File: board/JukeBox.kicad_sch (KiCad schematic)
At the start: 38 parts, among them J1 USB_C_Receptacle_USB2.0, SW1 SW_SPST, SW10 SW_SPST, SW11 SW_SPST, SW12 SW_SPST, SW2 SW_SPST, SW3 SW_SPST, SW4 SW_SPST, SW5 SW_SPST, SW6 SW_SPST, SW7 SW_SPST, SW8 SW_SPST, SW9 SW_SPST, U1 ATmega8U2-A, Y1 16MHz

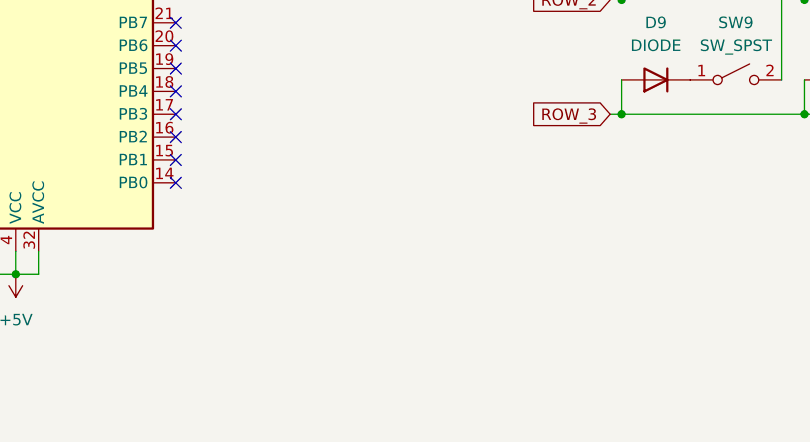
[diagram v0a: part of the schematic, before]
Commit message: update naming, add headers for direct connection
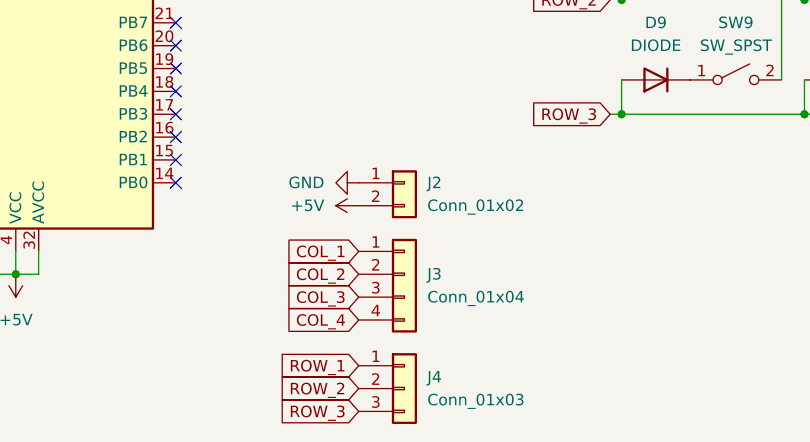
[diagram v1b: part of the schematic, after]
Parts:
- added J2: Conn_01x02, Connector_PinHeader_2.54mm:PinHeader_1x02_P2.54mm_Vertical, symbol Connector_Generic:Conn_01x02
- added J3: Conn_01x04, Connector_PinHeader_2.54mm:PinHeader_1x04_P2.54mm_Vertical, symbol Connector_Generic:Conn_01x04
- added J4: Conn_01x03, Connector_PinHeader_2.54mm:PinHeader_1x03_P2.54mm_Vertical, symbol Connector_Generic:Conn_01x03
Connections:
- net +5V: now also J2.2 (Pin_2)
- net COL_1: now also J3.1 (Pin_1)
- net COL_2: now also J3.2 (Pin_2)
- net COL_3: now also J3.3 (Pin_3)
- net COL_4: now also J3.4 (Pin_4)
- net GND: now also J2.1 (Pin_1)
- net ROW_1: now also J4.1 (Pin_1)
- net ROW_2: now also J4.2 (Pin_2)
- net ROW_3: now also J4.3 (Pin_3)
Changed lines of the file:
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@@
     (effects (font (size 1.27 1.27)) (justify left bottom))
+  )
+  (global_label "COL_4" (shape input) (at 158.75 111.76 180) (fields_autoplaced)
+    (effects (font (size 1.27 1.27)) (justify right))
+    (property "Intersheet References" "${INTERSHEET_REFS}" (id 0) (at 150.5312 111.6806 0)
+      (effects (font (size 1.27 1.27)) (justify right) hide)
+    )
   )
   (global_label "COL_1" (shape input) (at 138.43 53.34 0) (fields_autoplaced)
@@
     )
   )
+  (global_label "ROW_3" (shape input) (at 158.75 121.92 180) (fields_autoplaced)
+    (effects (font (size 1.27 1.27)) (justify right))
+    (property "Intersheet References" "${INTERSHEET_REFS}" (id 0) (at 150.1079 121.8406 0)
+      (effects (font (size 1.27 1.27)) (justify right) hide)
+    )
+  )
   (global_label "COL_2" (shape input) (at 224.79 49.53 180) (fields_autoplaced)
     (effects (font (size 1.27 1.27)) (justify right))
@@
     )
   )
+  (global_label "COL_2" (shape input) (at 158.75 106.68 180) (fields_autoplaced)
+    (effects (font (size 1.27 1.27)) (justify right))
+    (property "Intersheet References" "${INTERSHEET_REFS}" (id 0) (at 150.5312 106.6006 0)
+      (effects (font (size 1.27 1.27)) (justify right) hide)
+    )
+  )
   (global_label "ROW_2" (shape input) (at 186.69 76.2 180) (fields_autoplaced)
     (effects (font (size 1.27 1.27)) (justify right))
     (property "Intersheet References" "${INTERSHEET_REFS}" (id 0) (at 178.0479 76.1206 0)
+      (effects (font (size 1.27 1.27)) (justify right) hide)
+    )
+  )
+  (global_label "COL_1" (shape input) (at 158.75 104.14 180) (fields_autoplaced)
+    (effects (font (size 1.27 1.27)) (justify right))
+    (property "Intersheet References" "${INTERSHEET_REFS}" (id 0) (at 150.5312 104.0606 0)
+      (effects (font (size 1.27 1.27)) (justify right) hide)
+    )
+  )
+  (global_label "ROW_1" (shape input) (at 158.75 116.84 180) (fields_autoplaced)
+    (effects (font (size 1.27 1.27)) (justify right))
+    (property "Intersheet References" "${INTERSHEET_REFS}" (id 0) (at 150.1079 116.7606 0)
+      (effects (font (size 1.27 1.27)) (justify right) hide)
+    )
+  )
+  (global_label "COL_3" (shape input) (at 158.75 109.22 180) (fields_autoplaced)
+    (effects (font (size 1.27 1.27)) (justify right))
+    (property "Intersheet References" "${INTERSHEET_REFS}" (id 0) (at 150.5312 109.1406 0)
       (effects (font (size 1.27 1.27)) (justify right) hide)
     )
@@
     (property "Intersheet References" "${INTERSHEET_REFS}" (id 0) (at 147.0721 65.9606 0)
       (effects (font (size 1.27 1.27)) (justify left) hide)
+    )
+  )
+  (global_label "ROW_2" (shape input) (at 158.75 119.38 180) (fields_autoplaced)
+    (effects (font (size 1.27 1.27)) (justify right))
+    (property "Intersheet References" "${INTERSHEET_REFS}" (id 0) (at 150.1079 119.3006 0)
+      (effects (font (size 1.27 1.27)) (justify right) hide)
     )
   )
@@
     (pin "2")
   )
+  (symbol (lib_id "Connector_Generic:Conn_01x03") (at 163.83 119.38 0) (unit 1)
+    (in_bom yes) (on_board yes) (fields_autoplaced)
+    (property "Reference" "J4" (id 0) (at 166.37 118.1099 0)
+      (effects (font (size 1.27 1.27)) (justify left))
+    )
+    (property "Value" "Conn_01x03" (id 1) (at 166.37 120.6499 0)
+      (effects (font (size 1.27 1.27)) (justify left))
+    )
+    (property "Footprint" "Connector_PinHeader_2.54mm:PinHeader_1x03_P2.54mm_Vertical" (id 2) (at 163.83 119.38 0)
+      (effects (font (size 1.27 1.27)) hide)
+    )
+    (property "Datasheet" "~" (id 3) (at 163.83 119.38 0)
+      (effects (font (size 1.27 1.27)) hide)
+    )
+    (pin "1")
+    (pin "2")
+    (pin "3")
+  )
   (symbol (lib_id "power:GND") (at 100.33 63.5 180) (unit 1)
     (in_bom yes) (on_board yes) (fields_autoplaced)
@@
     )
     (pin "1")
+  )
+  (symbol (lib_id "Connector_Generic:Conn_01x04") (at 163.83 106.68 0) (unit 1)
+    (in_bom yes) (on_board yes) (fields_autoplaced)
+    (property "Reference" "J3" (id 0) (at 166.37 106.6799 0)
+      (effects (font (size 1.27 1.27)) (justify left))
+    )
+    (property "Value" "Conn_01x04" (id 1) (at 166.37 109.2199 0)
+      (effects (font (size 1.27 1.27)) (justify left))
+    )
+    (property "Footprint" "Connector_PinHeader_2.54mm:PinHeader_1x04_P2.54mm_Vertical" (id 2) (at 163.83 106.68 0)
+      (effects (font (size 1.27 1.27)) hide)
+    )
+    (property "Datasheet" "~" (id 3) (at 163.83 106.68 0)
+      (effects (font (size 1.27 1.27)) hide)
+    )
+    (pin "1")
+    (pin "2")
+    (pin "3")
+    (pin "4")
   )
   (symbol (lib_id "Switch:SW_SPST") (at 220.98 85.09 0) (unit 1)
@@
     (pin "2")
   )
+  (symbol (lib_id "power:+5V") (at 158.75 99.06 90) (unit 1)
+    (in_bom yes) (on_board yes) (fields_autoplaced)
+    (property "Reference" "#PWR?" (id 0) (at 162.56 99.06 0)
+      (effects (font (size 1.27 1.27)) hide)
+    )
+    (property "Value" "+5V" (id 1) (at 154.94 99.0599 90)
+      (effects (font (size 1.27 1.27)) (justify left))
+    )
+    (property "Footprint" "" (id 2) (at 158.75 99.06 0)
+      (effects (font (size 1.27 1.27)) hide)
+    )
+    (property "Datasheet" "" (id 3) (at 158.75 99.06 0)
+      (effects (font (size 1.27 1.27)) hide)
+    )
+    (pin "1")
+  )
   (symbol (lib_id "power:GND") (at 74.93 68.58 90) (unit 1)
     (in_bom yes) (on_board yes) (fields_autoplaced)
@@
     (pin "2")
   )
+  (symbol (lib_id "Connector_Generic:Conn_01x02") (at 163.83 96.52 0) (unit 1)
+    (in_bom yes) (on_board yes) (fields_autoplaced)
+    (property "Reference" "J2" (id 0) (at 166.37 96.5199 0)
+      (effects (font (size 1.27 1.27)) (justify left))
+    )
+    (property "Value" "Conn_01x02" (id 1) (at 166.37 99.0599 0)
+      (effects (font (size 1.27 1.27)) (justify left))
+    )
+    (property "Footprint" "Connector_PinHeader_2.54mm:PinHeader_1x02_P2.54mm_Vertical" (id 2) (at 163.83 96.52 0)
+      (effects (font (size 1.27 1.27)) hide)
+    )
+    (property "Datasheet" "~" (id 3) (at 163.83 96.52 0)
+      (effects (font (size 1.27 1.27)) hide)
+    )
+    (pin "1")
+    (pin "2")
+  )
   (symbol (lib_id "Simulation_SPICE:DIODE") (at 252.73 85.09 0) (unit 1)
     (in_bom yes) (on_board yes) (fields_autoplaced)
@@
     (pin "2")
   )
+  (symbol (lib_id "power:GND") (at 158.75 96.52 270) (unit 1)
+    (in_bom yes) (on_board yes) (fields_autoplaced)
+    (property "Reference" "#PWR?" (id 0) (at 152.4 96.52 0)
+      (effects (font (size 1.27 1.27)) hide)
+    )
+    (property "Value" "GND" (id 1) (at 154.94 96.5199 90)
+      (effects (font (size 1.27 1.27)) (justify right))
+    )
+    (property "Footprint" "" (id 2) (at 158.75 96.52 0)
+      (effects (font (size 1.27 1.27)) hide)
+    )
+    (property "Datasheet" "" (id 3) (at 158.75 96.52 0)
+      (effects (font (size 1.27 1.27)) hide)
+    )
+    (pin "1")
+  )
   (symbol (lib_id "power:GND") (at 266.7 40.64 180) (unit 1)
     (in_bom yes) (on_board yes)
@@
       (reference "#PWR0115") (unit 1) (value "+5V") (footprint "")
     )
+    (path "/bf8323cb-2b24-414a-8611-bcc957c5adee"
+      (reference "#PWR?") (unit 1) (value "+5V") (footprint "")
+    )
+    (path "/f342a1f0-e7c8-419d-bc73-21cafd1a5bd9"
+      (reference "#PWR?") (unit 1) (value "GND") (footprint "")
+    )
     (path "/9c9ee825-f2fc-4bed-8c37-591528a5e259"
       (reference "C1") (unit 1) (value "1uF") (footprint "Capacitor_THT:C_Disc_D5.0mm_W2.5mm_P5.00mm")
@@
       (reference "J1") (unit 1) (value "USB_C_Receptacle_USB2.0") (footprint "USB4085-GF-A:GCT_USB4085-GF-A_REVA4")
     )
+    (path "/d6465750-cb6e-4018-93ee-99d8be33c243"
+      (reference "J2") (unit 1) (value "Conn_01x02") (footprint "Connector_PinHeader_2.54mm:PinHeader_1x02_P2.54mm_Vertical")
+    )
+    (path "/6fbb616d-78b3-4e04-a633-0b4710aebc0f"
+      (reference "J3") (unit 1) (value "Conn_01x04") (footprint "Connector_PinHeader_2.54mm:PinHeader_1x04_P2.54mm_Vertical")
+    )
+    (path "/6c7eeabd-1949-4bca-9b3f-957472dee1b4"
+      (reference "J4") (unit 1) (value "Conn_01x03") (footprint "Connector_PinHeader_2.54mm:PinHeader_1x03_P2.54mm_Vertical")
+    )
     (path "/4557b69f-3b18-4afc-a8af-66203a6c8698"

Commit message: update footprints
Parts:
- J1: footprint USB4085-GF-A:GCT_USB4085-GF-A_REVA4 -> jukebox-footprints:GCT_USB4085-GF-A_REVA4
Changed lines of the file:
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@@
     (property "Reference" "J1" (id 0) (at 49.53 55.88 0))
     (property "Value" "USB_C_Receptacle_USB2.0" (id 1) (at 49.53 58.42 0))
-    (property "Footprint" "USB4085-GF-A:GCT_USB4085-GF-A_REVA4" (id 2) (at 53.34 78.74 0)
+    (property "Footprint" "jukebox-footprints:GCT_USB4085-GF-A_REVA4" (id 2) (at 53.34 78.74 0)
       (effects (font (size 1.27 1.27)) hide)
     )
@@
     )
     (path "/8bb352fe-5b3d-4124-a7b4-72612a8bc725"
-      (reference "J1") (unit 1) (value "USB_C_Receptacle_USB2.0") (footprint "USB4085-GF-A:GCT_USB4085-GF-A_REVA4")
+      (reference "J1") (unit 1) (value "USB_C_Receptacle_USB2.0") (footprint "jukebox-footprints:GCT_USB4085-GF-A_REVA4")
     )
     (path "/d6465750-cb6e-4018-93ee-99d8be33c243"

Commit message: add kailh choc switches in place of cherry mx's
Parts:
- SW1, SW10, SW11, SW12, SW2, SW3, SW4, SW5, SW6, SW7, SW8, SW9: footprint Button_Switch_Keyboard:SW_Cherry_MX_1.00u_PCB -> jukebox-footprints:Kailh_PG1350
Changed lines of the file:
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@@
     (property "Reference" "SW8" (id 0) (at 261.62 66.04 0))
     (property "Value" "SW_SPST" (id 1) (at 261.62 68.58 0))
-    (property "Footprint" "Button_Switch_Keyboard:SW_Cherry_MX_1.00u_PCB" (id 2) (at 261.62 72.39 0)
+    (property "Footprint" "jukebox-footprints:Kailh_PG1350" (id 2) (at 261.62 72.39 0)
       (effects (font (size 1.27 1.27)) hide)
     )
@@
     (property "Reference" "SW5" (id 0) (at 200.66 66.04 0))
     (property "Value" "SW_SPST" (id 1) (at 200.66 68.58 0))
-    (property "Footprint" "Button_Switch_Keyboard:SW_Cherry_MX_1.00u_PCB" (id 2) (at 200.66 72.39 0)
+    (property "Footprint" "jukebox-footprints:Kailh_PG1350" (id 2) (at 200.66 72.39 0)
       (effects (font (size 1.27 1.27)) hide)
     )
@@
     (property "Reference" "SW11" (id 0) (at 241.3 78.74 0))
     (property "Value" "SW_SPST" (id 1) (at 241.3 81.28 0))
-    (property "Footprint" "Button_Switch_Keyboard:SW_Cherry_MX_1.00u_PCB" (id 2) (at 241.3 85.09 0)
+    (property "Footprint" "jukebox-footprints:Kailh_PG1350" (id 2) (at 241.3 85.09 0)
       (effects (font (size 1.27 1.27)) hide)
     )
@@
     (property "Reference" "SW2" (id 0) (at 220.98 53.34 0))
     (property "Value" "SW_SPST" (id 1) (at 220.98 55.88 0))
-    (property "Footprint" "Button_Switch_Keyboard:SW_Cherry_MX_1.00u_PCB" (id 2) (at 220.98 59.69 0)
+    (property "Footprint" "jukebox-footprints:Kailh_PG1350" (id 2) (at 220.98 59.69 0)
       (effects (font (size 1.27 1.27)) hide)
     )
@@
     (property "Reference" "SW3" (id 0) (at 241.3 53.34 0))
     (property "Value" "SW_SPST" (id 1) (at 241.3 55.88 0))
-    (property "Footprint" "Button_Switch_Keyboard:SW_Cherry_MX_1.00u_PCB" (id 2) (at 241.3 59.69 0)
+    (property "Footprint" "jukebox-footprints:Kailh_PG1350" (id 2) (at 241.3 59.69 0)
       (effects (font (size 1.27 1.27)) hide)
     )
@@
     (property "Reference" "SW7" (id 0) (at 241.3 66.04 0))
     (property "Value" "SW_SPST" (id 1) (at 241.3 68.58 0))
-    (property "Footprint" "Button_Switch_Keyboard:SW_Cherry_MX_1.00u_PCB" (id 2) (at 241.3 72.39 0)
+    (property "Footprint" "jukebox-footprints:Kailh_PG1350" (id 2) (at 241.3 72.39 0)
       (effects (font (size 1.27 1.27)) hide)
     )
@@
     (property "Reference" "SW6" (id 0) (at 220.98 66.04 0))
     (property "Value" "SW_SPST" (id 1) (at 220.98 68.58 0))
-    (property "Footprint" "Button_Switch_Keyboard:SW_Cherry_MX_1.00u_PCB" (id 2) (at 220.98 72.39 0)
+    (property "Footprint" "jukebox-footprints:Kailh_PG1350" (id 2) (at 220.98 72.39 0)
       (effects (font (size 1.27 1.27)) hide)
     )
@@
     (property "Reference" "SW10" (id 0) (at 220.98 78.74 0))
     (property "Value" "SW_SPST" (id 1) (at 220.98 81.28 0))
-    (property "Footprint" "Button_Switch_Keyboard:SW_Cherry_MX_1.00u_PCB" (id 2) (at 220.98 85.09 0)
+    (property "Footprint" "jukebox-footprints:Kailh_PG1350" (id 2) (at 220.98 85.09 0)
       (effects (font (size 1.27 1.27)) hide)
     )
@@
     (property "Reference" "SW12" (id 0) (at 261.62 78.74 0))
     (property "Value" "SW_SPST" (id 1) (at 261.62 81.28 0))
-    (property "Footprint" "Button_Switch_Keyboard:SW_Cherry_MX_1.00u_PCB" (id 2) (at 261.62 85.09 0)
+    (property "Footprint" "jukebox-footprints:Kailh_PG1350" (id 2) (at 261.62 85.09 0)
       (effects (font (size 1.27 1.27)) hide)
     )
@@
     (property "Reference" "SW1" (id 0) (at 200.66 53.34 0))
     (property "Value" "SW_SPST" (id 1) (at 200.66 55.88 0))
-    (property "Footprint" "Button_Switch_Keyboard:SW_Cherry_MX_1.00u_PCB" (id 2) (at 200.66 59.69 0)
+    (property "Footprint" "jukebox-footprints:Kailh_PG1350" (id 2) (at 200.66 59.69 0)
       (effects (font (size 1.27 1.27)) hide)
     )
@@
     (property "Reference" "SW4" (id 0) (at 261.62 53.34 0))
     (property "Value" "SW_SPST" (id 1) (at 261.62 55.88 0))
-    (property "Footprint" "Button_Switch_Keyboard:SW_Cherry_MX_1.00u_PCB" (id 2) (at 261.62 59.69 0)
+    (property "Footprint" "jukebox-footprints:Kailh_PG1350" (id 2) (at 261.62 59.69 0)
       (effects (font (size 1.27 1.27)) hide)
     )
@@
     (property "Reference" "SW9" (id 0) (at 200.66 78.74 0))
     (property "Value" "SW_SPST" (id 1) (at 200.66 81.28 0))
-    (property "Footprint" "Button_Switch_Keyboard:SW_Cherry_MX_1.00u_PCB" (id 2) (at 200.66 85.09 0)
+    (property "Footprint" "jukebox-footprints:Kailh_PG1350" (id 2) (at 200.66 85.09 0)
       (effects (font (size 1.27 1.27)) hide)
     )
@@
     )
     (path "/9c521050-210b-4566-8df7-0c21d5047d29"
-      (reference "SW1") (unit 1) (value "SW_SPST") (footprint "Button_Switch_Keyboard:SW_Cherry_MX_1.00u_PCB")
+      (reference "SW1") (unit 1) (value "SW_SPST") (footprint "jukebox-footprints:Kailh_PG1350")
     )
     (path "/37c70e57-2ca6-421e-af79-c7e49f668aa3"
-      (reference "SW2") (unit 1) (value "SW_SPST") (footprint "Button_Switch_Keyboard:SW_Cherry_MX_1.00u_PCB")
+      (reference "SW2") (unit 1) (value "SW_SPST") (footprint "jukebox-footprints:Kailh_PG1350")
     )
     (path "/4b6c34fa-b1fb-45f3-a671-d72ce337273b"
-      (reference "SW3") (unit 1) (value "SW_SPST") (footprint "Button_Switch_Keyboard:SW_Cherry_MX_1.00u_PCB")
+      (reference "SW3") (unit 1) (value "SW_SPST") (footprint "jukebox-footprints:Kailh_PG1350")
     )
     (path "/c73ca981-71cf-4f32-b21e-3aa18b0f2771"
-      (reference "SW4") (unit 1) (value "SW_SPST") (footprint "Button_Switch_Keyboard:SW_Cherry_MX_1.00u_PCB")
+      (reference "SW4") (unit 1) (value "SW_SPST") (footprint "jukebox-footprints:Kailh_PG1350")
     )
     (path "/26d32f41-828d-4307-95a9-9b74b4fd95ff"
-      (reference "SW5") (unit 1) (value "SW_SPST") (footprint "Button_Switch_Keyboard:SW_Cherry_MX_1.00u_PCB")
+      (reference "SW5") (unit 1) (value "SW_SPST") (footprint "jukebox-footprints:Kailh_PG1350")
     )
     (path "/664de57e-5677-4997-b600-d19506285652"
-      (reference "SW6") (unit 1) (value "SW_SPST") (footprint "Button_Switch_Keyboard:SW_Cherry_MX_1.00u_PCB")
+      (reference "SW6") (unit 1) (value "SW_SPST") (footprint "jukebox-footprints:Kailh_PG1350")
     )
     (path "/4ca8ac79-2f84-470e-bb05-392315f9ca2d"
-      (reference "SW7") (unit 1) (value "SW_SPST") (footprint "Button_Switch_Keyboard:SW_Cherry_MX_1.00u_PCB")
+      (reference "SW7") (unit 1) (value "SW_SPST") (footprint "jukebox-footprints:Kailh_PG1350")
     )
     (path "/1e067fda-db48-429d-ab41-2684d67281ae"
-      (reference "SW8") (unit 1) (value "SW_SPST") (footprint "Button_Switch_Keyboard:SW_Cherry_MX_1.00u_PCB")
+      (reference "SW8") (unit 1) (value "SW_SPST") (footprint "jukebox-footprints:Kailh_PG1350")
     )
     (path "/e153897f-980c-4f95-9f21-744e2a4e8bfd"
-      (reference "SW9") (unit 1) (value "SW_SPST") (footprint "Button_Switch_Keyboard:SW_Cherry_MX_1.00u_PCB")
+      (reference "SW9") (unit 1) (value "SW_SPST") (footprint "jukebox-footprints:Kailh_PG1350")
     )
     (path "/764f050a-11e4-4b3b-944d-20a61d8045db"
-      (reference "SW10") (unit 1) (value "SW_SPST") (footprint "Button_Switch_Keyboard:SW_Cherry_MX_1.00u_PCB")
+      (reference "SW10") (unit 1) (value "SW_SPST") (footprint "jukebox-footprints:Kailh_PG1350")
     )
     (path "/34f0a189-60a5-4ee3-84c4-03829f6e40a8"
-      (reference "SW11") (unit 1) (value "SW_SPST") (footprint "Button_Switch_Keyboard:SW_Cherry_MX_1.00u_PCB")
+      (reference "SW11") (unit 1) (value "SW_SPST") (footprint "jukebox-footprints:Kailh_PG1350")
     )
     (path "/784822d3-acfc-4d8b-8e64-7ba82a312325"
-      (reference "SW12") (unit 1) (value "SW_SPST") (footprint "Button_Switch_Keyboard:SW_Cherry_MX_1.00u_PCB")
+      (reference "SW12") (unit 1) (value "SW_SPST") (footprint "jukebox-footprints:Kailh_PG1350")
     )
     (path "/2a6075ae-c7fa-41db-86b8-3f996740bdc2"

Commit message: update models
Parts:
- Y1: footprint Crystal:Crystal_HC18-U_Vertical -> Crystal:Crystal_HC49-4H_Vertical
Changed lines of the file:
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@@
       (effects (font (size 1.27 1.27)) (justify right))
     )
-    (property "Footprint" "Crystal:Crystal_HC18-U_Vertical" (id 2) (at 99.06 88.9 0)
+    (property "Footprint" "Crystal:Crystal_HC49-4H_Vertical" (id 2) (at 99.06 88.9 0)
       (effects (font (size 1.27 1.27)) hide)
     )
@@
     )
     (path "/79e6aeff-a19c-4b10-b09f-51af268e6bfb"
-      (reference "Y1") (unit 1) (value "16MHz") (footprint "Crystal:Crystal_HC18-U_Vertical")
-    )
-  )
+      (reference "Y1") (unit 1) (value "16MHz") (footprint "Crystal:Crystal_HC49-4H_Vertical")
+    )
+  )
